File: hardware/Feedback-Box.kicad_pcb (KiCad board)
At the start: 2 copper layers, 100 x 50 mm, 87 parts, among them J1 694106301002, J2 UJ2-BH-1-TH, J3 T821106A1S100CEU, J4 SSW-104-01-T-S, Q1 FDN340P, Q2 FDN340P, Q3 MMBT2222ALT1G, Q4 FDN340P, Q5 FDN340P, Q6 FDN340P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

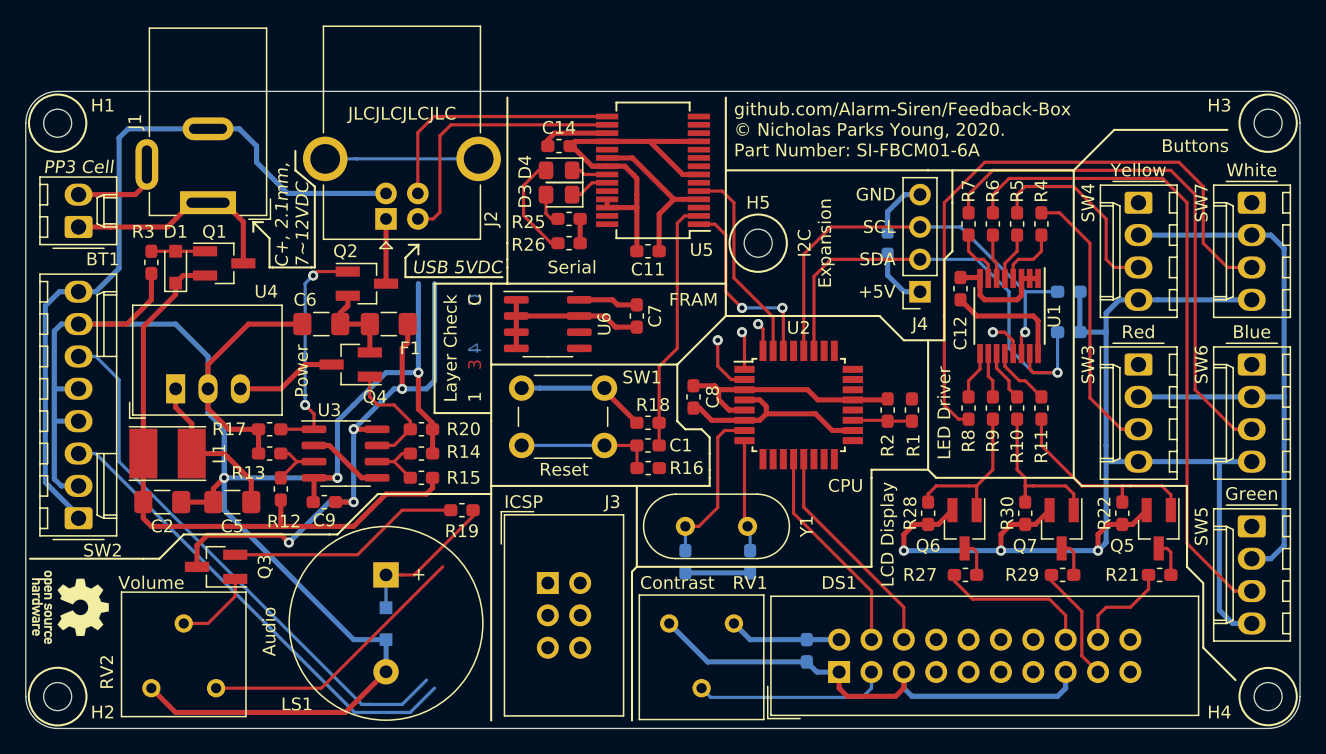
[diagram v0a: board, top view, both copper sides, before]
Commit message: Finish Layout
Finished PCB layout;
Also added another decoupling cap for the ICSP;
Also added (C) info to schematic + layout;
Also added Chris' name as "checked by".
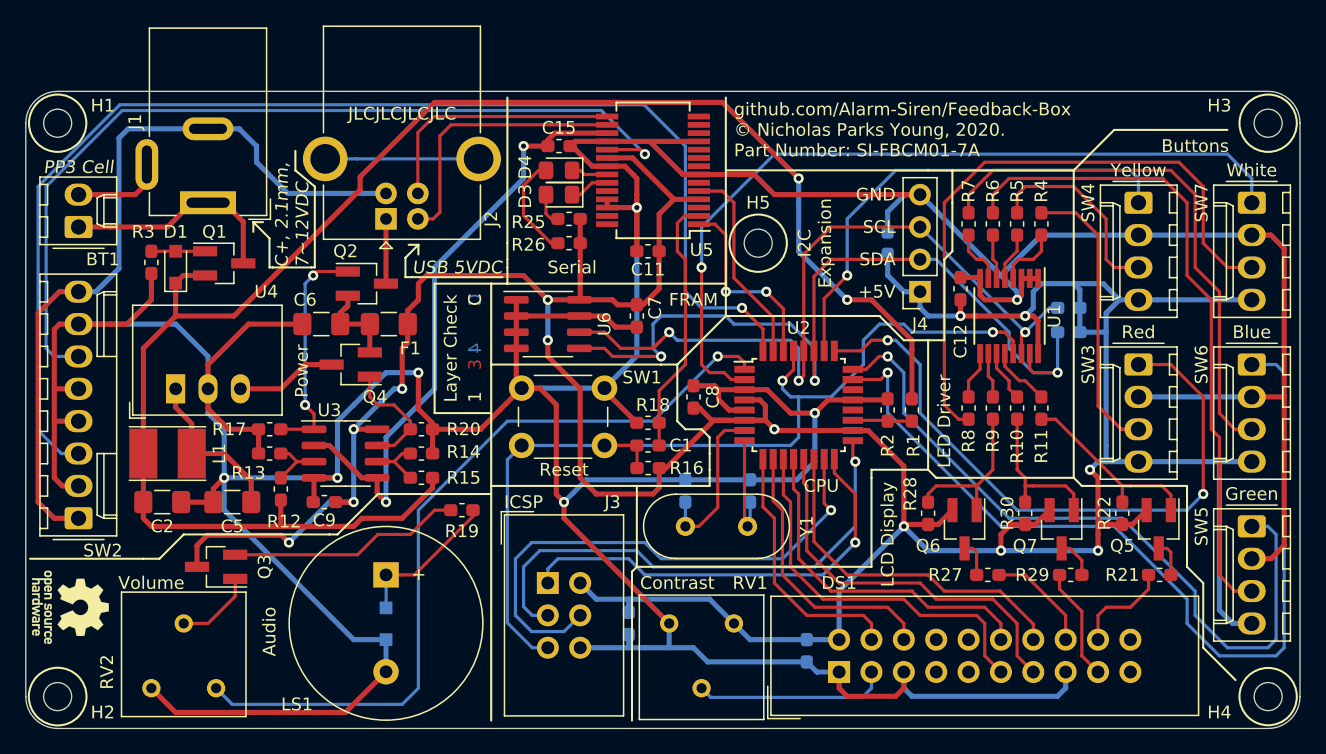
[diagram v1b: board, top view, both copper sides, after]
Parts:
- added C14: 100n, Capacitor_SMD:C_0603_1608Metric_Pad1.05x0.95mm_HandSolder, B.Cu at (147.3, 111.8)
- G1: footprint Feedback-Box:SI-Logo-W32.5mm_H13.5mm -> Feedback-Box:SI-Logo-W20.3mm_H8.4mm
- moved G1 42.2 mm to (175.9, 98.4)
- moved C3 5.56 mm to (151.8, 101.4), turned to 270 degrees
- moved C4 5.56 mm to (156.8, 101.4), turned to 270 degrees
- moved R27 1.75 mm to (175.5, 108.0), turned to 0 degrees
- moved R24 1.27 mm to (181.8, 87.0)
- moved R29 0.63 mm to (182.0, 108.0)
- renumbered C14 to C15
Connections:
- U2 pad 1: BTN1 -> SPK
- U2 pad 10: BTN4 -> LCD_E
- U2 pad 11: BTN5 -> LCD_D4
- U2 pad 12: LCD_RS -> LCD_D5
- U2 pad 13: LCD_E -> LCD_D6
- U2 pad 14: SPK -> LCD_D7
- U2 pad 2: BTN2 -> BTN5
- U2 pad 23: LCD_D4 -> BTN4
- U2 pad 24: LCD_D5 -> BTN3
- U2 pad 25: LCD_D6 -> BTN1
- U2 pad 26: LCD_D7 -> BTN2
- U2 pad 9: BTN3 -> LCD_RS
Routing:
- net GND: track 335.4 -> 450.6 mm, vias 3 -> 7
- net +5V: track 199.3 -> 297.5 mm, vias 7 -> 13
- net BAT: track 49.1 -> 130.1 mm, vias 0 -> 2
- net BTN4: track 0.00 -> 70.9 mm, vias 0 -> 1
- net BTN5: track 0.00 -> 62.9 mm, vias 0 -> 1
- net ~RST: track 13.7 -> 74.6 mm, vias 1 -> 2
- net PROG~EN: track 39.4 -> 98.3 mm
- net BTN3: track 0.00 -> 56.8 mm, vias 0 -> 1
- net BTN1: track 3.00 -> 51.3 mm, vias 1 -> 2
- net /MOSI: track 0.00 -> 42.2 mm, vias 0 -> 1
- net /SCLK: track 0.00 -> 40.5 mm, vias 0 -> 1
- net SPK: track 21.7 -> 62.2 mm, vias 0 -> 1
- net +3V3: track 11.4 -> 47.9 mm, vias 0 -> 2
- net /MISO: track 0.00 -> 34.4 mm, vias 0 -> 1
- net BTN2: track 4.56 -> 37.7 mm
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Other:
- board text added: "github.com/Alarm-Siren/Feedback-Box © Nicholas Parks Young, 2020. Part Number: SI-FBCM01-7A"
- board text removed: "github.com/Alarm-Siren/Feedback-Box © Nicholas Parks Young, 2020. Part Number: SI-FBCM01-6A"

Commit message: Added RST+TX+RX to Expansion Header
Added RST, and Serial TXD/RXD to the Expansion header. To allow TXD/RXD from the FT232RL to be safely 'overriden' by an expansion device, two additional 1K resistors have been fitted as well.
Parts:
- added G3: OSHW-Logo_5.7x6mm_SilkScreen, Symbol:OSHW-Logo_5.7x6mm_SilkScreen, B.Cu at (103.5, 110.5)
- added R31: 1k, Resistor_SMD:R_0603_1608Metric_Pad1.05x0.95mm_HandSolder, B.Cu at (157.5, 85.1)
- added R32: 1k, Resistor_SMD:R_0603_1608Metric_Pad1.05x0.95mm_HandSolder, B.Cu at (160.7, 80.6)
- J4: value SSW-104-01-T-S -> SSW-107-01-T-S; footprint Connector_PinSocket_2.54mm:PinSocket_1x04_P2.54mm_Vertical -> Connector_PinSocket_2.54mm:PinSocket_1x07_P2.54mm_Vertical
- moved C13 1.91 mm to (167.6, 80.0)
- moved H5 1.91 mm to (157.5, 80.0)
- moved J4 1.91 mm to (170.2, 87.6)
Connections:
- J4 pad 4: GND -> ~RST
- U5 pad 1: RXD -> Net-(R31-Pad2)
- U5 pad 5: TXD -> Net-(R32-Pad2)
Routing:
- net ~RST: track 74.6 -> 92.2 mm
- net Net-(R32-Pad2): track 0.00 -> 9.53 mm, vias 0 -> 1
- net BTN2: track 37.7 -> 46.4 mm, vias 1 -> 3
- net GND: track 450.6 -> 459.3 mm
- net TXD: track 16.0 -> 23.3 mm, vias 0 -> 1
- net BTN5: track 62.9 -> 70.0 mm
- net Net-(R31-Pad2): track 0.00 -> 6.97 mm, vias 0 -> 1
- net RXD: track 15.3 -> 21.4 mm, vias 2 -> 1
- net SCL: track 59.1 -> 55.3 mm
- net SDA: track 65.0 -> 62.0 mm
- net +5V: track 297.5 -> 299.8 mm
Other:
- board text added: "Expansion Header"
- board text added: "P.No. SI-FBCM01-8A © See Reverse"
- board text added: "RXD"
- board text added: "TXD"
- board text added: "github.com/Alarm-Siren/Feedback-Box © Nicholas Parks Young, 2020. Part Number: SI-FBCM01-8A"
- board text added: "~RST"
- board text removed: "I2C Expansion"
- board text removed: "github.com/Alarm-Siren/Feedback-Box © Nicholas Parks Young, 2020. Part Number: SI-FBCM01-7A"
